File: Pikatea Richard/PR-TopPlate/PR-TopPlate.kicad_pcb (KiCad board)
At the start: 2 copper layers, 62 x 136.7 mm, 7 parts, among them SW1 Rotary_Encoder_Switch, SW2 Rotary_Encoder_Switch

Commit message: updated footprints added gerbers
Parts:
- moved SW1 2.00 mm to (155.0, 100.0)
- moved SW2 2.00 mm to (123.0, 100.0)
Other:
- board size 62 x 136.7 mm -> 66 x 138.1 mm

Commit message: update universal libraries
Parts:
- removed MX1, MX2, MX3, MX4, MX5: MX-LED, MX_Only:MXOnly-1U-Hotswap-Antishear
- removed SW1, SW2: Rotary_Encoder_Switch, Pikatea Macropad Encoder Side Mount:Encoder-BI_EN11_HSM0E
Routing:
- added copper zone on B.Cu, net (none)
- added copper zone on F.Cu, net (none)
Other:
- outline, holes or cut-outs redrawn

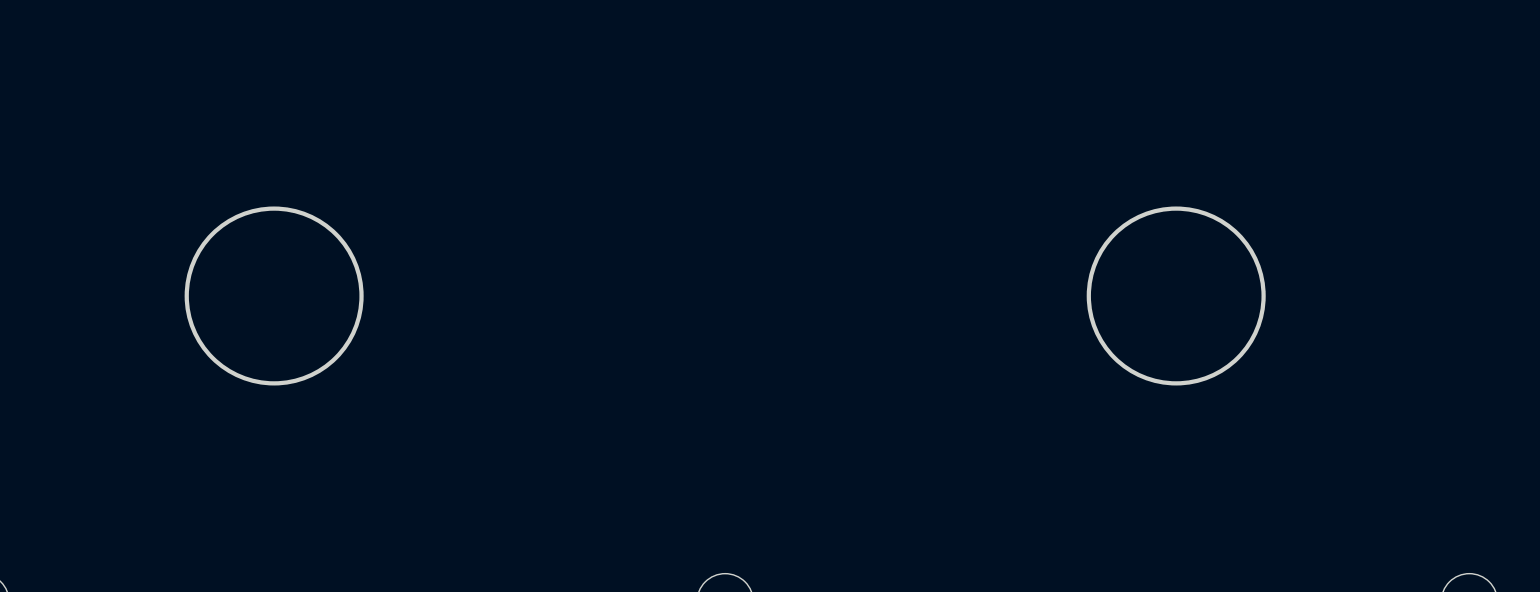
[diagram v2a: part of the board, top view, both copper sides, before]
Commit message: update keyboard
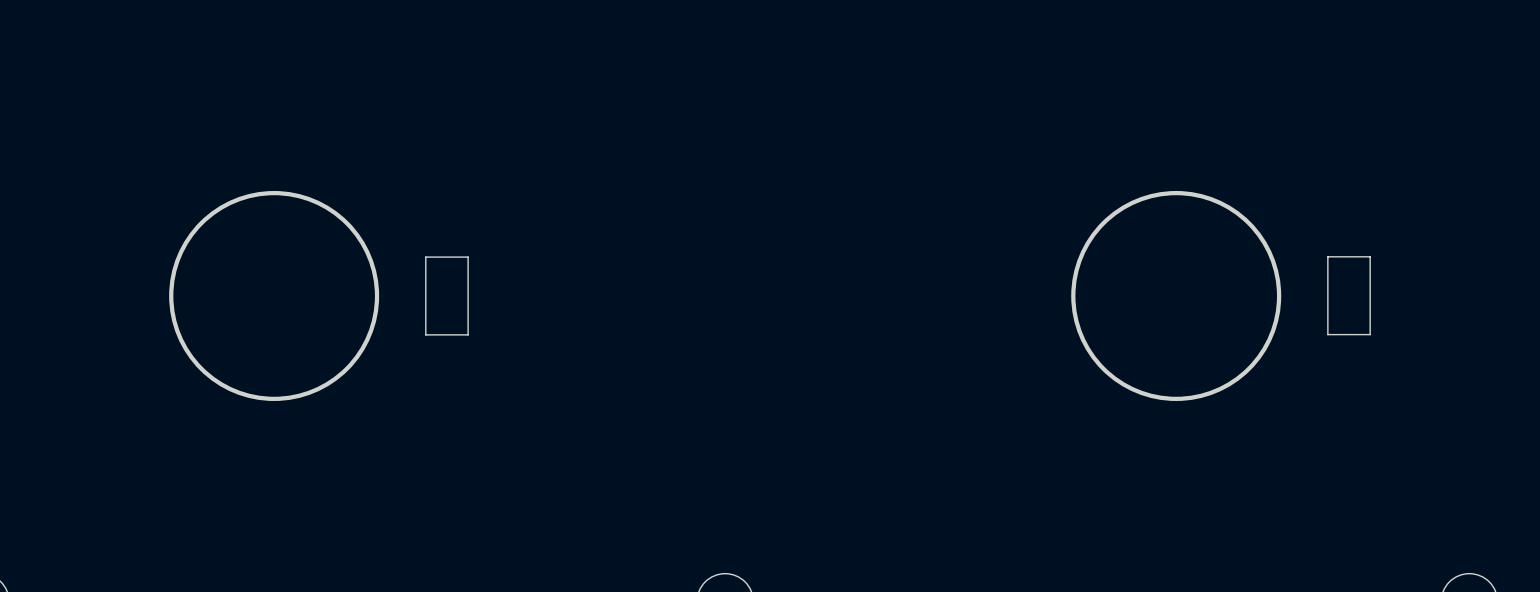
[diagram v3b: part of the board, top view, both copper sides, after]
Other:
- outline, holes or cut-outs redrawn
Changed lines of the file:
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@@
   (general
     (thickness 1.6)
-    (drawings 64)
+    (drawings 72)
     (tracks 0)
     (zones 0)
@@
     (uvia_drill 0.1)
   )
+  (gr_line (start 161.88 98.61) (end 160.38 98.61) (layer Edge.Cuts) (width 0.05))
+  (gr_line (start 161.88 101.37) (end 161.88 98.61) (layer Edge.Cuts) (width 0.05))
+  (gr_line (start 160.38 101.37) (end 161.88 101.37) (layer Edge.Cuts) (width 0.05))
+  (gr_line (start 160.38 98.61) (end 160.38 101.37) (layer Edge.Cuts) (width 0.05))
+  (gr_line (start 129.88 98.62) (end 128.38 98.62) (layer Edge.Cuts) (width 0.05))
+  (gr_line (start 129.88 101.38) (end 129.88 98.62) (layer Edge.Cuts) (width 0.05))
+  (gr_line (start 128.38 101.38) (end 129.88 101.38) (layer Edge.Cuts) (width 0.05))
+  (gr_line (start 128.38 98.62) (end 128.38 101.38) (layer Edge.Cuts) (width 0.05))
   (gr_line (start 139 110.85) (end 112.6 110.85) (layer Dwgs.User) (width 0.15))
   (gr_circle (center 112.6 110.85) (end 111.6 110.85) (layer Edge.Cuts) (width 0.05))
@@
   (gr_line (start 148.5 83.4) (end 129.5 83.4) (layer Dwgs.User) (width 0.15))
   (gr_circle (center 155 100) (end 166 100) (layer Dwgs.User) (width 0.15))
-  (gr_circle (center 155 100) (end 158.1 100) (layer Edge.Cuts) (width 0.15))
-  (gr_circle (center 123 100) (end 126.1 100) (layer Edge.Cuts) (width 0.15))
+  (gr_circle (center 155 100) (end 158.65 100) (layer Edge.Cuts) (width 0.15))
+  (gr_circle (center 123 100) (end 126.65 100) (layer Edge.Cuts) (width 0.15))
   (gr_circle (center 123 100) (end 134 100) (layer Dwgs.User) (width 0.15))
   (zone (net 0) (net_name "") (layer F.Cu) (hatch edge 0.508)
